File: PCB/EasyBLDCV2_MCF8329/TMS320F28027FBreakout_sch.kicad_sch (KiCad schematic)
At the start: 29 parts, among them U1 MCF8329A1IREER

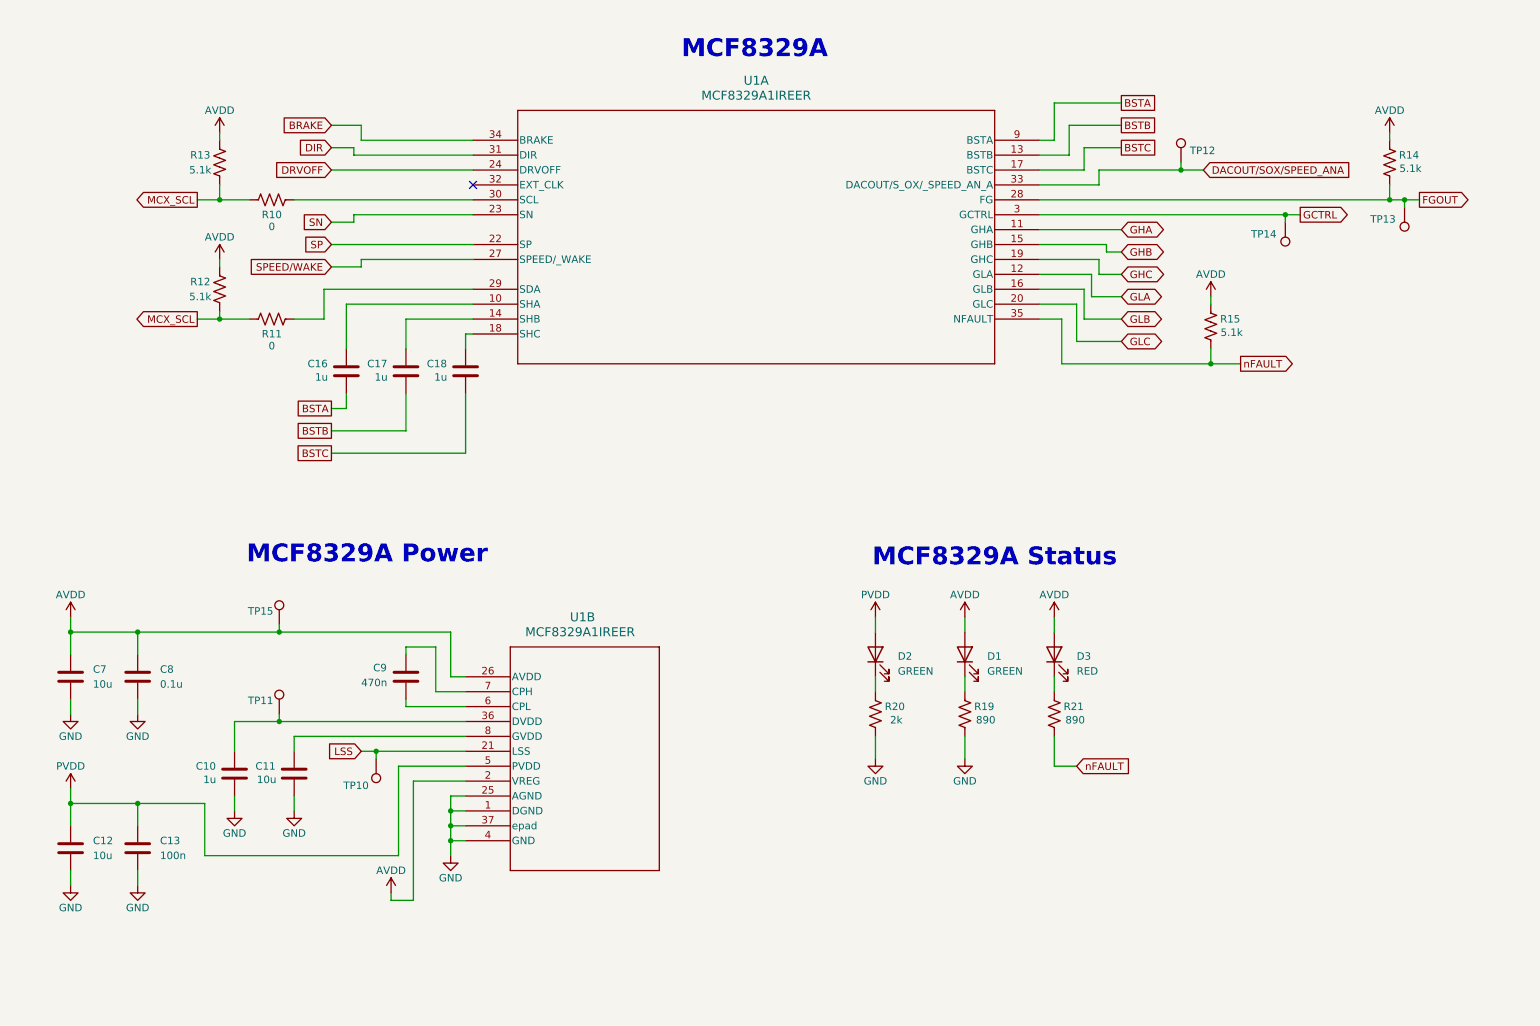
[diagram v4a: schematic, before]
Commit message: Assigned footprints, created bom
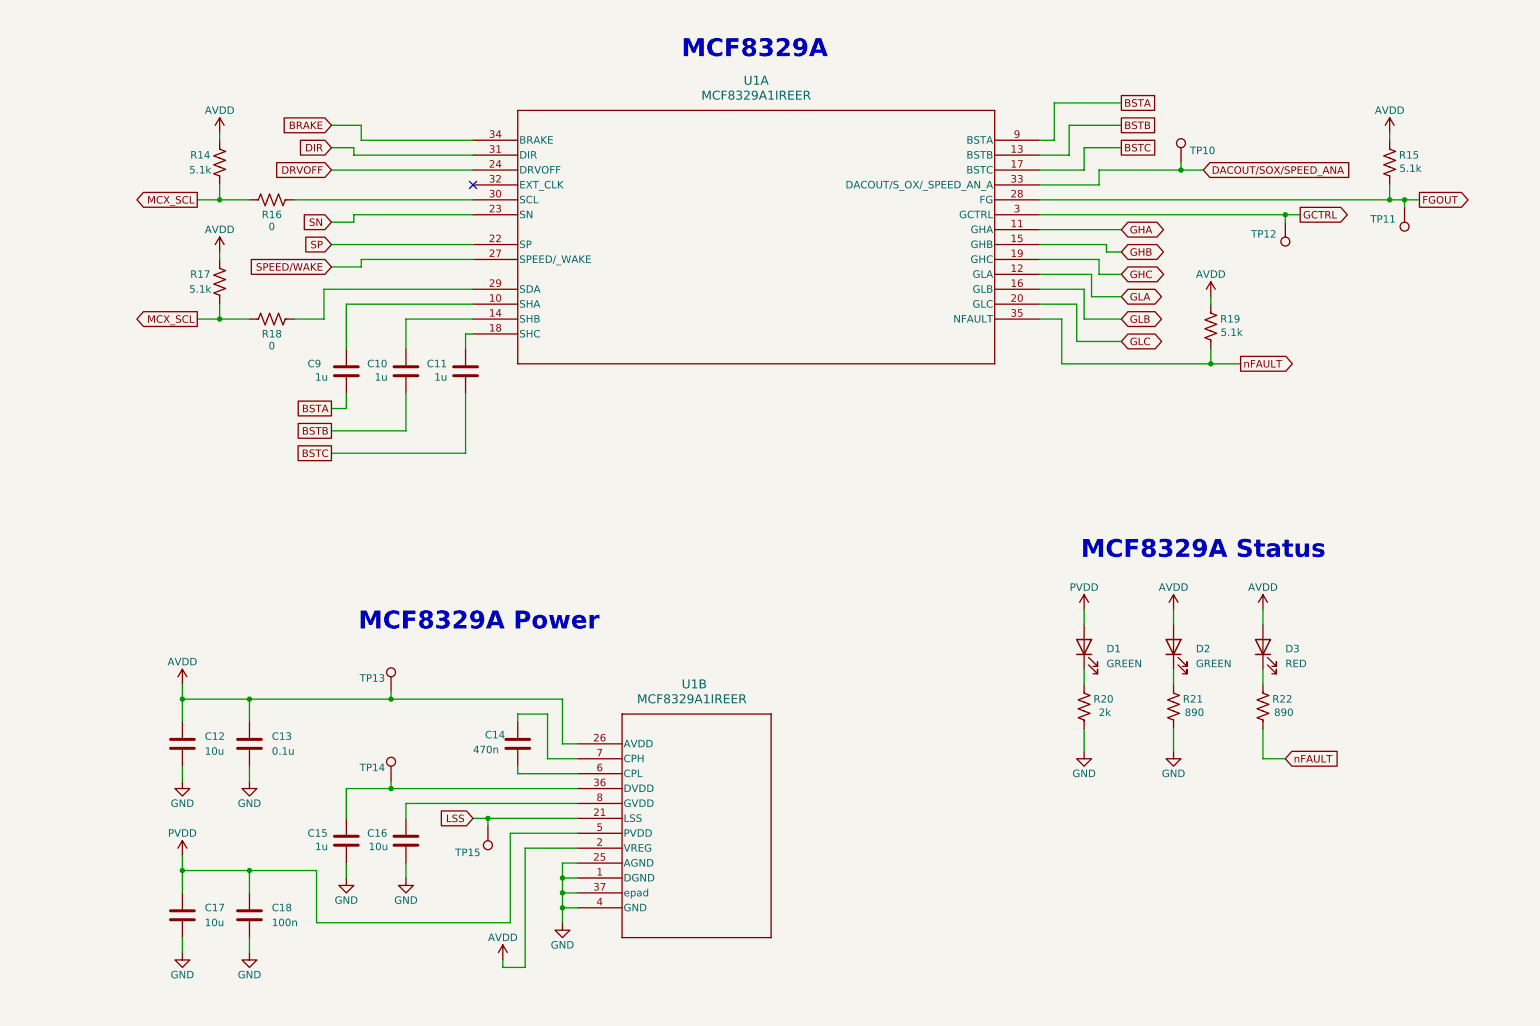
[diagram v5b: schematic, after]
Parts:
- C10: renamed from C17; footprint (none) -> Capacitor_SMD:C_0603_1608Metric
- C11: renamed from C18; footprint (none) -> Capacitor_SMD:C_0603_1608Metric
- C12: renamed from C7; footprint (none) -> Capacitor_SMD:C_0603_1608Metric
- C13: renamed from C8; footprint (none) -> Capacitor_SMD:C_0603_1608Metric
- C14: renamed from C9; footprint (none) -> Capacitor_SMD:C_0805_2012Metric
- C15: renamed from C10; footprint (none) -> Capacitor_SMD:C_0603_1608Metric
- C16: renamed from C11; footprint (none) -> Capacitor_SMD:C_0603_1608Metric
- C17: renamed from C12; footprint (none) -> Capacitor_SMD:C_2220_5750Metric
- C18: renamed from C13; footprint (none) -> Capacitor_SMD:C_0603_1608Metric
- C9: renamed from C16; footprint (none) -> Capacitor_SMD:C_0603_1608Metric
- D1: renamed from D2; footprint (none) -> LED_SMD:LED_0805_2012Metric
- D2: renamed from D1; footprint (none) -> LED_SMD:LED_0805_2012Metric
- D3: footprint (none) -> LED_SMD:LED_0805_2012Metric
- R14: renamed from R13; footprint (none) -> Resistor_SMD:R_0603_1608Metric
- R15: renamed from R14; footprint (none) -> Resistor_SMD:R_0603_1608Metric
- R16: renamed from R10; footprint (none) -> Resistor_SMD:R_0603_1608Metric
- R17: renamed from R12; footprint (none) -> Resistor_SMD:R_0603_1608Metric
- R18: renamed from R11; footprint (none) -> Resistor_SMD:R_0603_1608Metric
- R19: renamed from R15; footprint (none) -> Resistor_SMD:R_0603_1608Metric
- R20: footprint (none) -> Resistor_SMD:R_0603_1608Metric
- R21: renamed from R19; footprint (none) -> Resistor_SMD:R_0603_1608Metric
- R22: renamed from R21; footprint (none) -> Resistor_SMD:R_0603_1608Metric
- TP10: renamed from TP12; footprint (none) -> TestPoint:TestPoint_Pad_D1.5mm
- TP11: renamed from TP13; footprint (none) -> TestPoint:TestPoint_Pad_D1.5mm
- TP12: renamed from TP14; footprint (none) -> TestPoint:TestPoint_Pad_D1.5mm
- TP13: renamed from TP15; footprint (none) -> TestPoint:TestPoint_Pad_D1.5mm
- TP14: renamed from TP11; footprint (none) -> TestPoint:TestPoint_Pad_D1.5mm
- TP15: renamed from TP10; footprint (none) -> TestPoint:TestPoint_Pad_D1.5mm
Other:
- moved on the sheet: C12, C13, C14, C15, C16, C17, C18, D1, D2, D3, R17, R20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

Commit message: More work on layout
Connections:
- net GHA renamed GH_A
- net GHB renamed GH_B
- net GHC renamed GH_C
- net GLA renamed GL_A
- net GLB renamed GL_B
- net GLC renamed GL_C
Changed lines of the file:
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@@
 		)
 	)
-	(global_label "GHC"
+	(global_label "GH_C"
 		(shape bidirectional)
 		(at 205.74 59.69 0)
@@
 		)
 		(property "Intersheetrefs" "${INTERSHEET_REFS}"
-			(at 213.707 59.69 0)
+			(at 214.6746 59.69 0)
 			(effects
 				(font
@@
 		)
 	)
-	(global_label "GLA"
+	(global_label "GL_A"
 		(shape bidirectional)
 		(at 205.74 63.5 0)
@@
 		)
 		(property "Intersheetrefs" "${INTERSHEET_REFS}"
-			(at 213.2232 63.5 0)
+			(at 214.1908 63.5 0)
 			(effects
 				(font
@@
 		)
 	)
-	(global_label "GHB"
+	(global_label "GH_B"
 		(shape bidirectional)
 		(at 205.74 55.88 0)
@@
 		)
 		(property "Intersheetrefs" "${INTERSHEET_REFS}"
-			(at 213.707 55.88 0)
+			(at 214.6746 55.88 0)
 			(effects
 				(font
@@
 		)
 	)
-	(global_label "GLC"
+	(global_label "GL_C"
 		(shape bidirectional)
 		(at 205.74 71.12 0)
@@
 		)
 		(property "Intersheetrefs" "${INTERSHEET_REFS}"
-			(at 213.4046 71.12 0)
+			(at 214.3722 71.12 0)
 			(effects
 				(font
@@
 		)
 	)
-	(global_label "GLB"
+	(global_label "GL_B"
 		(shape bidirectional)
 		(at 205.74 67.31 0)
@@
 		)
 		(property "Intersheetrefs" "${INTERSHEET_REFS}"
-			(at 213.4046 67.31 0)
-			(effects
-				(font
-					(size 1.27 1.27)
-				)
-				(justify left)
-				(hide yes)
-			)
-		)
-	)
-	(global_label "GHA"
+			(at 214.3722 67.31 0)
+			(effects
+				(font
+					(size 1.27 1.27)
+				)
+				(justify left)
+				(hide yes)
+			)
+		)
+	)
+	(global_label "GH_A"
 		(shape bidirectional)
 		(at 205.74 52.07 0)
@@
 		)
 		(property "Intersheetrefs" "${INTERSHEET_REFS}"
-			(at 213.5256 52.07 0)
-			(effects
-				(font
+			(at 214.4932 52.07 0)
+			(effects
+				(font

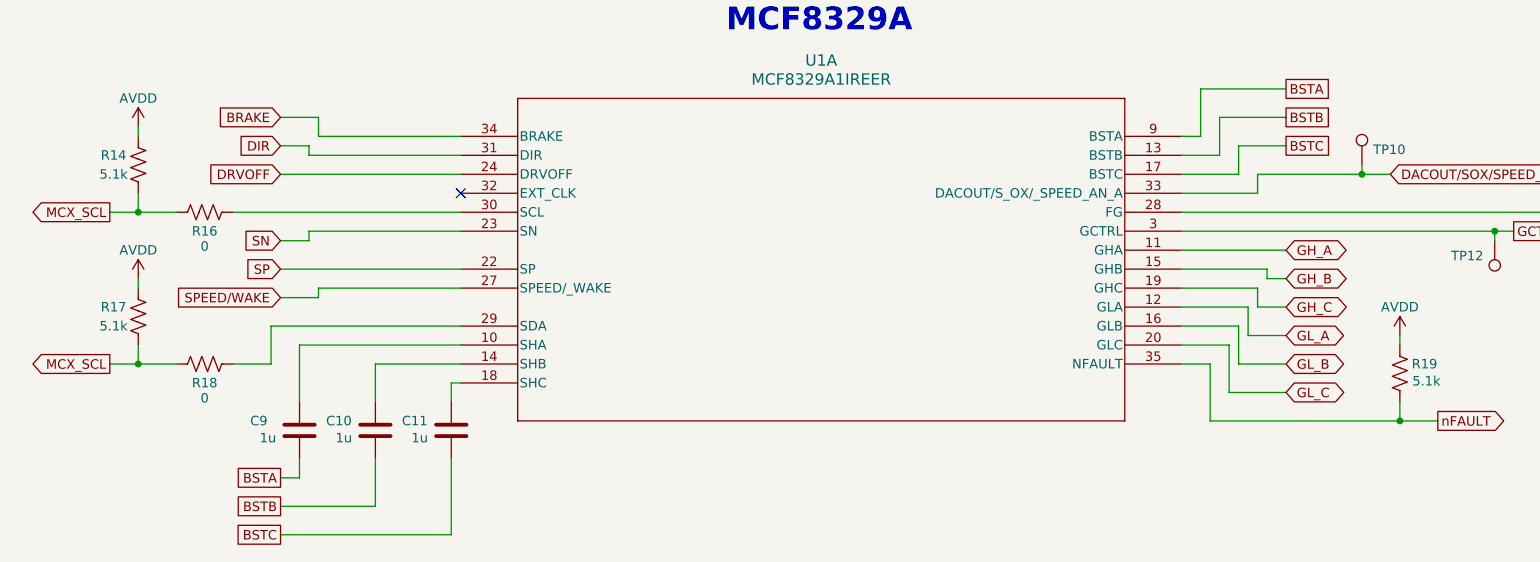
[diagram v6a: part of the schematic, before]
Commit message: Finished Silscreen
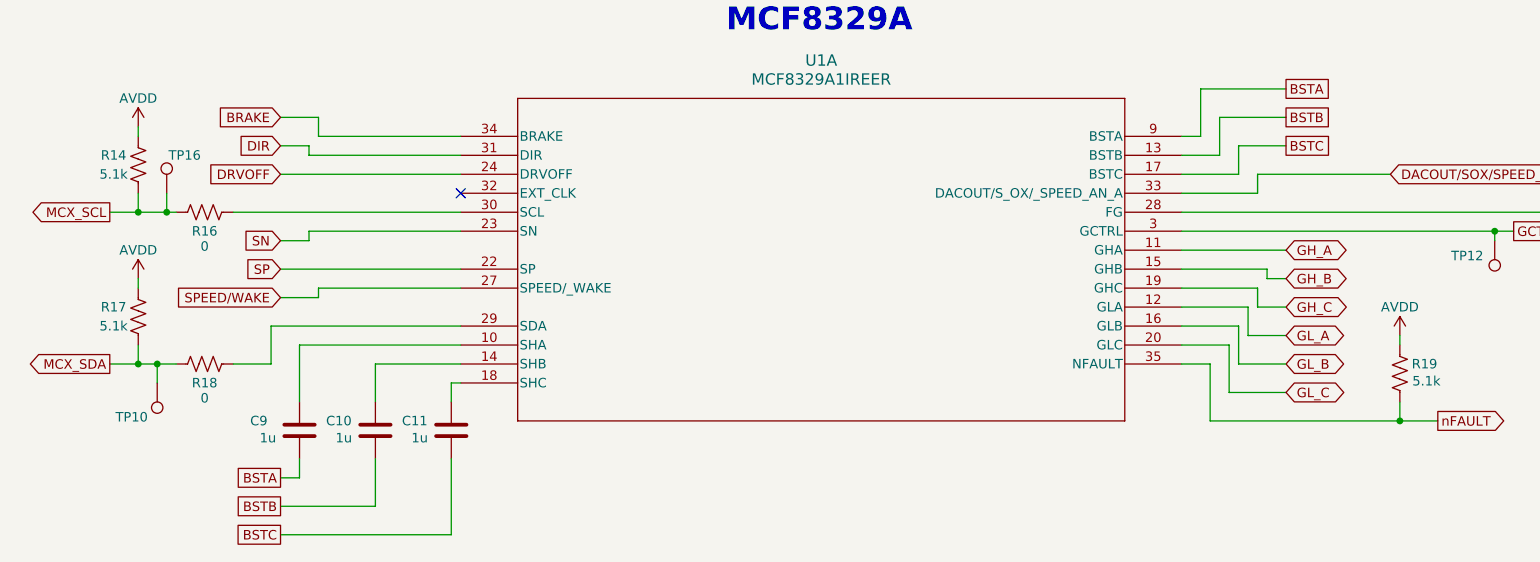
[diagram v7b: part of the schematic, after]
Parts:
- added TP16: TestPoint, TestPoint:TestPoint_Pad_D1.5mm, symbol Connector:TestPoint
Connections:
- net DACOUT/SOX/SPEED_ANA: no longer TP10.1
- net MCX_SCL: now also TP16.1; no longer R17.1, R18.1
- new net MCX_SDA: R17.1, R18.1, TP10.1
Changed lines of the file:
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@@
 	)
 	(junction
+		(at 54.61 67.31)
+		(diameter 0)
+		(color 0 0 0 0)
+	)
+	(junction
+		(at 55.88 46.99)
+		(diameter 0)
+		(color 0 0 0 0)
+	)
+	(junction
 		(at 52.07 46.99)
 		(diameter 0)
@@
 	)
 	(junction
-		(at 215.9 41.91)
-		(diameter 0)
-		(color 0 0 0 0)
-	)
-	(junction
 		(at 81.28 147.32)
 		(diameter 0)
@@
 	(wire
 		(pts
+			(xy 55.88 44.45) (xy 55.88 46.99)
+		)
+		(stroke
+			(width 0)
+			(type default)
+		)
+	)
+	(wire
+		(pts
 			(xy 48.26 67.31) (xy 52.07 67.31)
 		)
@@
 	(wire
 		(pts
-			(xy 215.9 41.91) (xy 219.71 41.91)
+			(xy 201.93 41.91) (xy 219.71 41.91)
 		)
 		(stroke
@@
 	(wire
 		(pts
+			(xy 54.61 67.31) (xy 57.15 67.31)
+		)
+		(stroke
+			(width 0)
+			(type default)
+		)
+	)
+	(wire
+		(pts
 			(xy 110.49 167.64) (xy 110.49 165.1)
 		)
@@
 	(wire
 		(pts
-			(xy 201.93 41.91) (xy 215.9 41.91)
-		)
-		(stroke
-			(width 0)
-			(type default)
-		)
-	)
-	(wire
-		(pts
 			(xy 191.77 39.37) (xy 196.85 39.37)
 		)
@@
 	(wire
 		(pts
-			(xy 215.9 40.64) (xy 215.9 41.91)
-		)
-		(stroke
-			(width 0)
-			(type default)
-		)
-	)
-	(wire
-		(pts
 			(xy 251.46 35.56) (xy 251.46 36.83)
 		)
@@
 	(wire
 		(pts
+			(xy 55.88 46.99) (xy 57.15 46.99)
+		)
+		(stroke
+			(width 0)
+			(type default)
+		)
+	)
+	(wire
+		(pts
 			(xy 113.03 167.64) (xy 110.49 167.64)
 		)
@@
 	(wire
 		(pts
-			(xy 52.07 46.99) (xy 57.15 46.99)
+			(xy 52.07 46.99) (xy 55.88 46.99)
 		)
 		(stroke
@@
 	(wire
 		(pts
+			(xy 54.61 67.31) (xy 54.61 69.85)
+		)
+		(stroke
+			(width 0)
+			(type default)
+		)
+	)
+	(wire
+		(pts
 			(xy 101.6 154.94) (xy 101.6 170.18)
 		)
@@
 	(wire
 		(pts
-			(xy 52.07 67.31) (xy 57.15 67.31)
+			(xy 52.07 67.31) (xy 54.61 67.31)
 		)
 		(stroke
@@
 		)
 	)
-	(global_label "MCX_SCL"
+	(global_label "MCX_SDA"
 		(shape output)
 		(at 48.26 67.31 180)
@@
 		)
 		(property "Intersheetrefs" "${INTERSHEET_REFS}"
-			(at 36.8687 67.31 0)
+			(at 36.8082 67.31 0)
 			(effects
 				(font
@@
 	)
 	(symbol
+		(lib_id "Connector:TestPoint")
+		(at 54.61 69.85 180)
+		(unit 1)
+		(exclude_from_sim no)
+		(in_bom yes)
+		(on_board yes)
+		(dnp no)
+		(property "Reference" "TP10"
+			(at 49.022 74.422 0)
+			(effects
+				(font
+					(size 1.27 1.27)
+				)
+				(justify right)
+			)
+		)
+		(property "Value" "TestPoint"
+			(at 57.15 74.4219 0)
+			(effects
+				(font
+					(size 1.27 1.27)
+				)
+				(justify right)
+				(hide yes)
+			)
+		)
+		(property "Footprint" "TestPoint:TestPoint_Pad_D1.5mm"
+			(at 49.53 69.85 0)
+			(effects
+				(font
+					(size 1.27 1.27)
+				)
+				(hide yes)
+			)
+		)
+		(property "Datasheet" "~"
+			(at 49.53 69.85 0)
+			(effects
+				(font
+					(size 1.27 1.27)
+				)
+				(hide yes)
+			)
+		)
+		(property "Description" "test point"
+			(at 54.61 69.85 0)
+			(effects
+				(font
+					(size 1.27 1.27)
+				)
+				(hide yes)
+			)
+		)
+		(pin "1"
+		)
+		(instances
+			(project "EasyBLDCV2_MCF8329"
+				(path "/6c304649-7c80-4a4c-b925-07b9210ad53d/8049925a-2faa-4187-b86e-b6208aed2e10"
+					(reference "TP10")
+					(unit 1)
+				)
+			)
+		)
+	)
+	(symbol
 		(lib_id "power:+1V1")
 		(at 229.87 116.84 0)
@@
 	)
 	(symbol
+		(lib_id "Connector:TestPoint")
+		(at 55.88 44.45 0)
+		(unit 1)
+		(exclude_from_sim no)
+		(in_bom yes)
+		(on_board yes)
+		(dnp no)
+		(property "Reference" "TP16"
+			(at 60.452 39.37 0)
+			(effects
+				(font
+					(size 1.27 1.27)
+				)
+				(justify right)
+			)
+		)
+		(property "Value" "TestPoint"
+			(at 53.34 39.8781 0)
+			(effects
+				(font
+					(size 1.27 1.27)
+				)
+				(justify right)
+				(hide yes)
+			)
+		)
+		(property "Footprint" "TestPoint:TestPoint_Pad_D1.5mm"
+			(at 60.96 44.45 0)
+			(effects
+				(font
+					(size 1.27 1.27)
+				)
+				(hide yes)
+			)
+		)
+		(property "Datasheet" "~"
+			(at 60.96 44.45 0)
+			(effects
+				(font
+					(size 1.27 1.27)
+				)
+				(hide yes)
+			)
+		)
+		(property "Description" "test point"
+			(at 55.88 44.45 0)
+			(effects
+				(font
+					(size 1.27 1.27)
+				)
+				(hide yes)
+			)
+		)
+		(pin "1"
+		)
+		(instances
+			(project "EasyBLDCV2_MCF8329"
+				(path "/6c304649-7c80-4a4c-b925-07b9210ad53d/8049925a-2faa-4187-b86e-b6208aed2e10"
+					(reference "TP16")
+					(unit 1)
+				)
+			)
+		)
+	)
+	(symbol
 		(lib_id "Device:C")
 		(at 83.82 156.21 0)
@@
 	(symbol
 		(lib_id "Connector:TestPoint")
-		(at 215.9 40.64 0)
-		(unit 1)
-		(exclude_from_sim no)
-		(in_bom yes)
-		(on_board yes)
-		(dnp no)
-		(property "Reference" "TP10"
-			(at 221.742 38.608 0)
-			(effects
-				(font
-					(size 1.27 1.27)
-				)
-				(justify right)
-			)
-		)
-		(property "Value" "TestPoint"
-			(at 213.36 36.0681 0)
-			(effects
-				(font
-					(size 1.27 1.27)
-				)
-				(justify right)
-				(hide yes)
-			)
-		)
-		(property "Footprint" "TestPoint:TestPoint_Pad_D1.5mm"
-			(at 220.98 40.64 0)
-			(effects
-				(font
-					(size 1.27 1.27)
-				)
-				(hide yes)
-			)
-		)
-		(property "Datasheet" "~"
-			(at 220.98 40.64 0)
-			(effects
-				(font
-					(size 1.27 1.27)
-				)
-				(hide yes)
-			)
-		)
-		(property "Description" "test point"
-			(at 215.9 40.64 0)
-			(effects
-				(font
-					(size 1.27 1.27)
-				)
-				(hide yes)
-			)
-		)
-		(pin "1"
-		)
-		(instances
-			(project "EasyBLDCV2_MCF8329"
-				(path "/6c304649-7c80-4a4c-b925-07b9210ad53d/8049925a-2faa-4187-b86e-b6208aed2e10"
-					(reference "TP10")
-					(unit 1)
-				)
-			)
-		)
-	)
-	(symbol
-		(lib_id "Connector:TestPoint")
 		(at 254 48.26 180)
 		(unit 1)
@@
 		(on_board yes)
 		(dnp no)
-		(fields_autoplaced yes)
 		(property "Reference" "U1"
 			(at 143.51 26.67 0)
